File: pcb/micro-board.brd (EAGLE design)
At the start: 127 x 76.2 mm, 113 parts, among them IC1 STM32F401RET6U, IC2 LDS3985M33R, IC3 LDS3985M33R, IC4 HX711, IC5 TLV2462IP, J12 B2B-PH-K-S_LF__SN_, J14 3V3 LED, J15 VDDA LED, J16 HX711 LED, J18 DC Power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

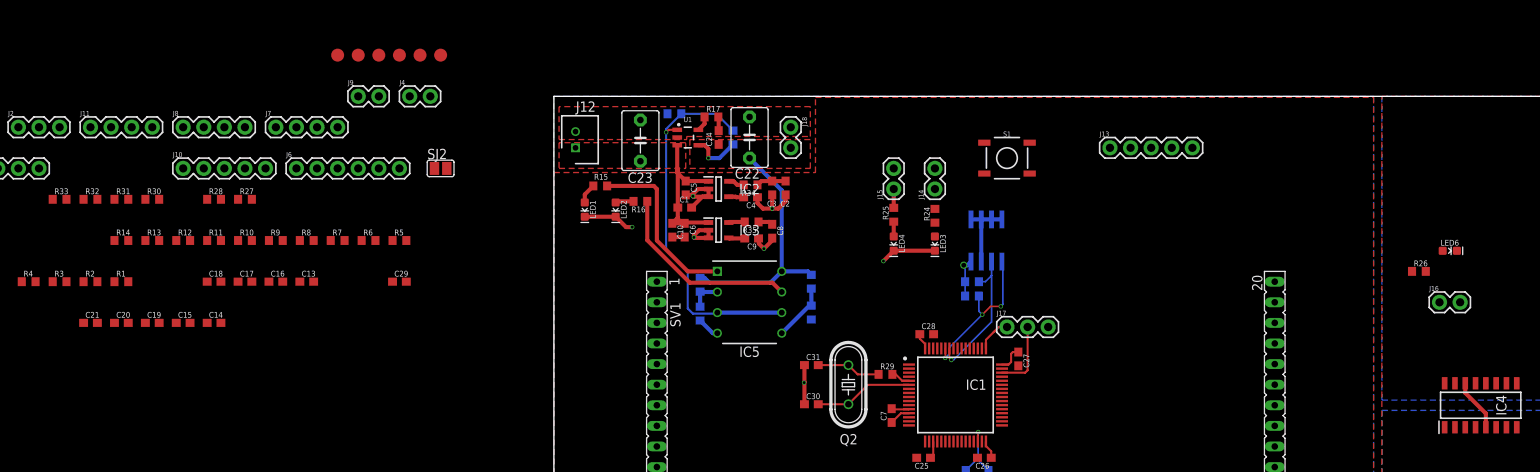
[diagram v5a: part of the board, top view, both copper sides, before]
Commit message: Continued Routing (more in longer description)
Added these subsystems routed:
nrst for reset switch.
HXDATA and HXCLK for the Micro's header.
Boot0 pad
Scope probe headers for GND and 3.3V
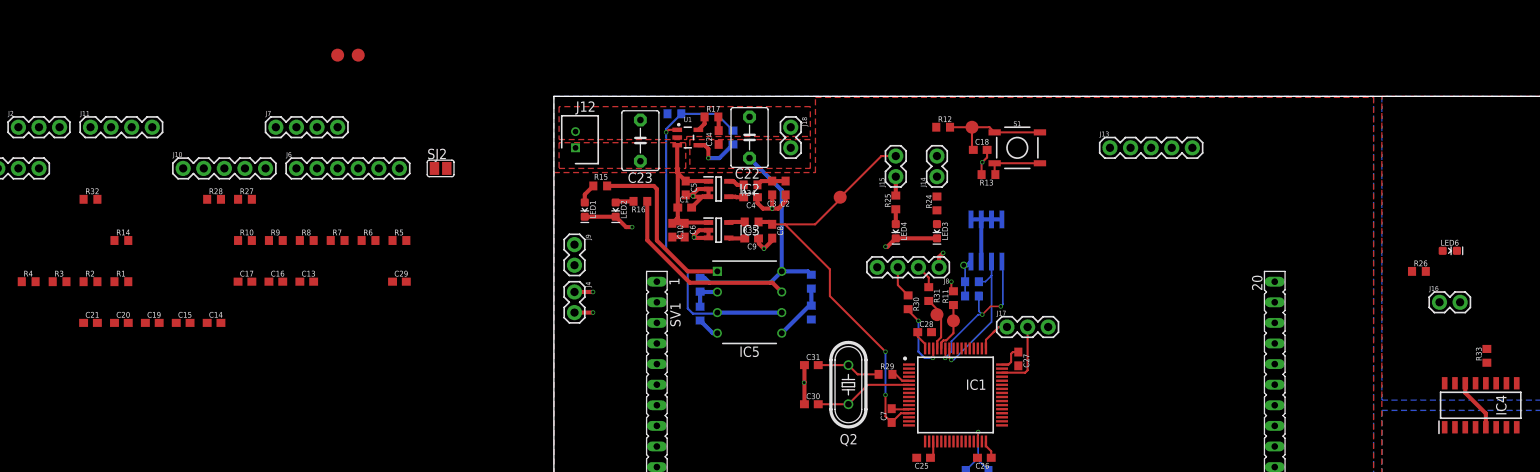
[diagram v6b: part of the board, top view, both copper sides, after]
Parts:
- moved R33 177.1 mm to (115.1, 44.2), turned to 90 degrees
- moved R13 103.4 mm to (53.6, 66.5), turned to 180 degrees
- moved R31 100.3 mm to (46.2, 51.8), turned to 270 degrees
- moved C18 95.9 mm to (52.6, 69.6)
- moved J8 94.8 mm to (47.5, 55.1), turned to 180 degrees
- moved R12 94.8 mm to (48.0, 72.4)
- moved R30 94.1 mm to (43.7, 50.8), turned to 270 degrees
- moved R11 91.5 mm to (49.3, 51.3), turned to 90 degrees
- moved U$4 73.5 mm to (49.3, 48.5)
- moved U$5 71.2 mm to (51.6, 72.4)
- moved U$3 69.1 mm to (47.2, 49.3)
- moved U$6 59.5 mm to (35.3, 63.8)
- moved J9 32.3 mm to (2.54, 57.9), turned to 270 degrees
- moved J4 31.5 mm to (2.54, 52.1), turned to 270 degrees
- moved S1 1.80 mm to (57.1, 69.8)
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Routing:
- net VDDA: track 4.42 -> 53.2 mm, vias 0 -> 2
- net NRST: track 0.00 -> 14.2 mm
- net GND: track 66.5 -> 77.6 mm, vias 7 -> 12
- net HXCLK_P: track 0.00 -> 9.05 mm, vias 0 -> 2
- net N$17: track 0.00 -> 7.02 mm
- net HXDATA_P: track 0.00 -> 6.68 mm
- net BOOT0: track 0.00 -> 6.18 mm
- net HXCLK: track 0.00 -> 3.99 mm
- net HXDATA: track 0.00 -> 2.98 mm

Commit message: Updated TFT right-side header, debug headers, and routing
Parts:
- removed J10: (no value), LinnesLab-Connectors:1X05
- added C32: 0.1uF, LinnesLab-Passives:C0603
- added R38, R39: 10k, LinnesLab-Passives:R0603
- added TFT: (no value), LinnesLab-Connectors:1X05
- R27: value 470 -> 1k
- moved SJ1 223.9 mm to (148.1, 23.4)
- moved R32 218.4 mm to (159.0, 32.0)
- moved R27 191.5 mm to (151.1, 34.0)
- moved R28 187.5 mm to (141.5, 24.6)
- moved C19 187.5 mm to (136.9, 28.7)
- moved C17 184.0 mm to (142.2, 17.0)
- moved C29 179.4 mm to (157.5, 21.6)
- moved U$1 178.3 mm to (97.8, 27.2)
- moved R7 175.0 mm to (146.1, 30.5)
- moved R8 173.7 mm to (141.5, 34.0)
- moved SJ2 171.7 mm to (152.9, 26.9)
- moved J11 157.4 mm to (94.7, 31.0), turned to 90 degrees
- moved J7 156.1 mm to (114.3, 24.6)
- moved U$8 144.2 mm to (108.0, 29.5)
- moved J1 141.3 mm to (69.8, 57.7)
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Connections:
- net N$8 renamed VCAP1
- new net IM2: R38.2, SV2.5
- new net IM3: R39.2, SV2.6
- net 3.3V: now also C32.2, R38.1, R39.1, R6.1
- net GND: now also C32.1; no longer R6.1
- net NC_MISO: now also J6.4; no longer J6.5
- net SS_CS: now also J6.2; no longer J6.3
- net SS_MOSI: now also J6.5; no longer J6.4
- net SS_SCK: now also J6.3; no longer J6.2
- net TFT_CS: now also TFT.4; no longer J10.4
- net TFT_DC: now also TFT.5; no longer J10.5
- net TFT_MISO: now also TFT.2; no longer J10.2
- net TFT_MOSI: now also TFT.3; no longer J10.3
- net TFT_SCK: now also TFT.1; no longer J10.1
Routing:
- net TFT_CS: track 0.00 -> 61.1 mm
- net Y+: track 0.00 -> 51.8 mm, vias 0 -> 1
- net TFT_SCK: track 0.00 -> 51.5 mm
- net X-: track 0.00 -> 50.3 mm, vias 0 -> 1
- net Y-: track 0.00 -> 50.1 mm, vias 0 -> 1
- net X+: track 0.00 -> 49.9 mm, vias 0 -> 1
- net TFT_MISO: track 0.00 -> 48.1 mm
- net TFT_MOSI: track 0.00 -> 47.3 mm
- net LITE: track 0.00 -> 47.3 mm, vias 0 -> 1
- net TFT_DC: track 0.00 -> 45.4 mm
- net PC0: track 0.00 -> 44.9 mm, vias 0 -> 1
- net PC3: track 0.00 -> 44.8 mm
- net PC2: track 0.00 -> 44.5 mm
- net PC1: track 0.00 -> 44.3 mm
- net SD_CS: track 0.00 -> 42.9 mm
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- added copper zone on layer 1, net 3.3V
- removed copper zone on layer 1, net 3V3
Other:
- board text added: "3V3"
- board text added: "CS"
- board text added: "D/C"
- board text added: "GND"
- board text added: "MISO"
- board text added: "MOSI"
- board text added: "PC0"
- board text added: "PC1"
- board text added: "PC2"
- board text added: "PC3"
- board text added: "SCK"
- board text added: "TP4"
- board text added: "X+"
- board text added: "X-"
- board text added: "Y+"
- board text added: "Y-"
- board text added: "~CS"

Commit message: Incremental commit of changes made
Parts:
- added C33: 0.1uF, LinnesLab-Passives:C0603
- added C34: 10uF, LinnesLab-Passives:C0603
- moved C15 157.3 mm to (110.7, 31.8), flipped to the bottom, turned to 180 degrees
- moved C16 146.4 mm to (110.7, 33.5), flipped to the bottom, turned to 180 degrees
- moved C20 73.5 mm to (17.5, 67.8)
- moved R32 51.3 mm to (109.5, 45.5), turned to 180 degrees
- moved J5 46.1 mm to (104.6, 50.8), turned to 270 degrees
- moved SJ2 39.9 mm to (119.4, 48.5)
- moved SJ1 36.2 mm to (119.4, 45.5)
- moved R27 31.9 mm to (123.4, 49.8), flipped to the bottom, turned to 270 degrees
- moved C17 30.9 mm to (115.3, 32.3)
- moved C29 30.4 mm to (136.7, 43.7)
- moved R7 28.0 mm to (118.1, 29.2), turned to 270 degrees
- moved R28 27.6 mm to (123.4, 45.5), turned to 180 degrees
- moved R8 22.1 mm to (119.9, 29.2), turned to 270 degrees
- moved C19 18.5 mm to (118.9, 32.8)
- moved J16 8.03 mm to (104.6, 57.4), turned to 90 degrees
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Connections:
- net 3.3V: now also C33.1, C34.1
- net GND: now also C33.2, C34.2
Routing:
- net AVDD: track 0.00 -> 25.8 mm
- net V_BASE: track 0.00 -> 24.3 mm
- net GND: track 93.2 -> 113.7 mm, vias 12 -> 16
- net N$12: track 0.00 -> 13.2 mm, vias 0 -> 2
- net CH-: track 0.00 -> 11.2 mm
- net CH+: track 0.00 -> 11.0 mm
- net HXDATA: track 2.98 -> 13.0 mm
- net HX_CLK: track 0.00 -> 8.58 mm, vias 0 -> 2
- net 3.3V: track 30.3 -> 35.5 mm, vias 1 -> 2
- net HX_SDA: track 0.00 -> 4.68 mm
- net HXCLK: track 3.99 -> 8.08 mm
- net HX_LED: track 0.00 -> 3.90 mm
- net A-: track 0.00 -> 3.63 mm
- net N$10: track 0.00 -> 3.48 mm, vias 0 -> 1
- net A+: track 0.00 -> 3.32 mm
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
